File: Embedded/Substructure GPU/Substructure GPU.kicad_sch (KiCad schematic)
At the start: 30 parts, among them J1 10171746-00021LF, J11 Substructure Power, J2 HUB75, J3 5V, U2 74HC245D_653, U3 74HC245D_653, U5 Substructure, U6 LD1117S33TR_SOT223, U7 LD1117S50TR_SOT223

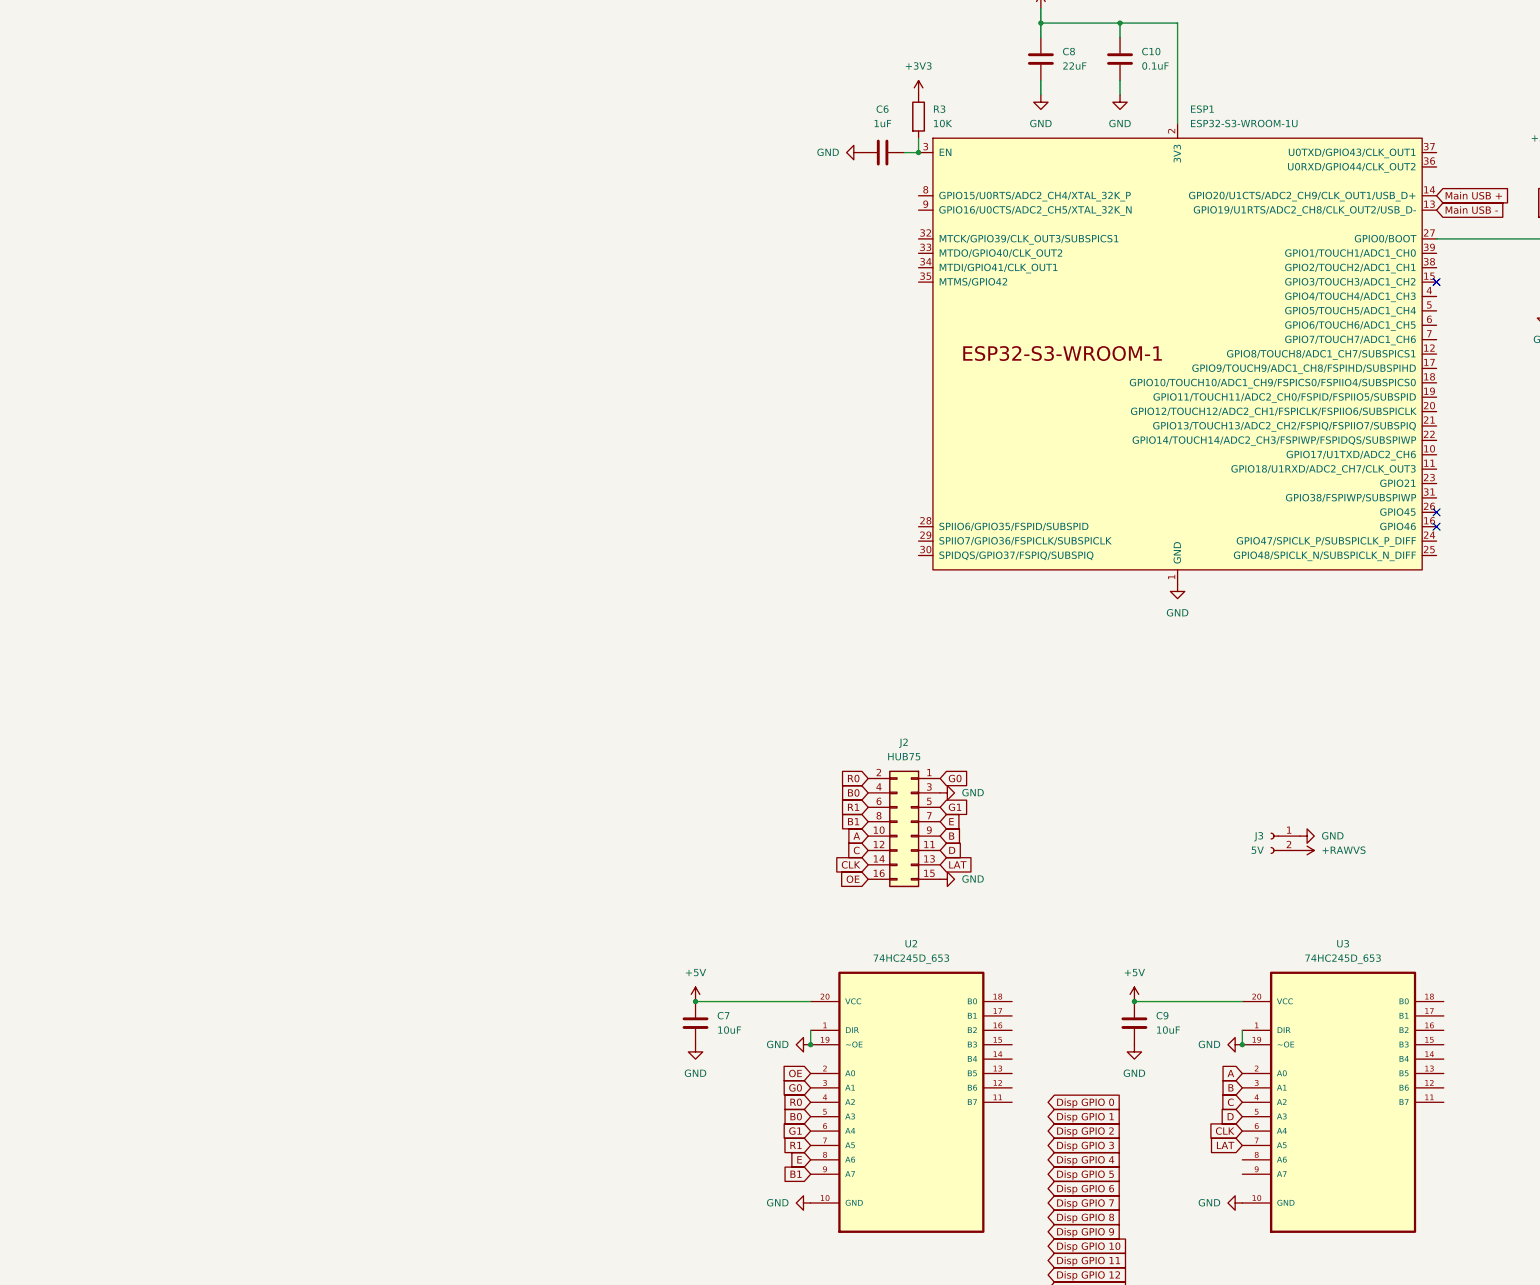
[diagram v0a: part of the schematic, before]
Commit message: Added Component placement for main systems
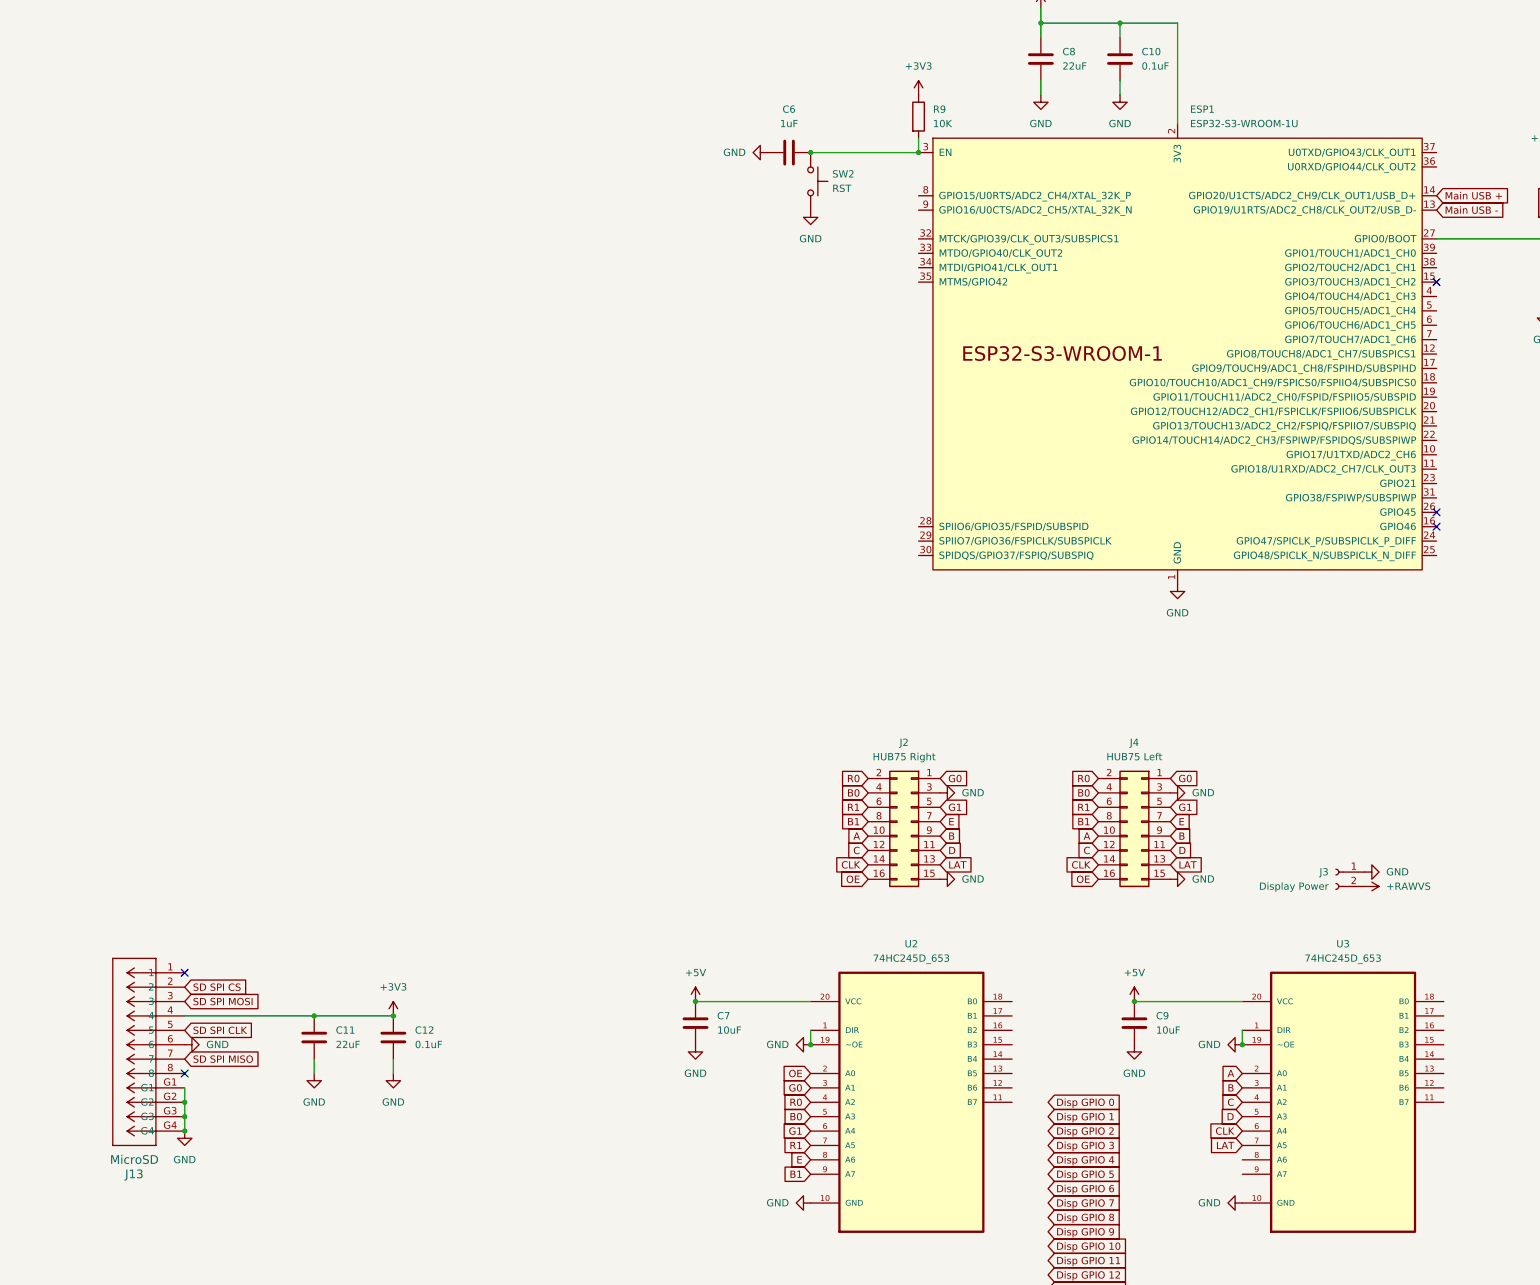
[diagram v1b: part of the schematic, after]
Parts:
- added C11: 22uF, Capacitor_SMD:C_0603_1608Metric_Pad1.08x0.95mm_HandSolder, symbol Device:C
- added C12: 0.1uF, Capacitor_SMD:C_0603_1608Metric_Pad1.08x0.95mm_HandSolder, symbol Device:C
- added J13: MicroSD, Micro SD:MicroSD_473092651, symbol MicroSD_473092651:473092651
- added J4: HUB75 Left, Connector_PinHeader_2.54mm:PinHeader_2x08_P2.54mm_Vertical, symbol Connector_Generic:Conn_02x08_Odd_Even
- added SW2: RST, Buttons:R-667843, symbol Switch:SW_Push
- J11: footprint Connector_AMASS:AMASS_XT30PW-M_1x02_P2.50mm_Horizontal -> Connector_AMASS:AMASS_XT30U-M_1x02_P5.0mm_Vertical
- J2: value HUB75 -> HUB75 Right
- J3: value 5V -> Display Power; footprint Connector_AMASS:AMASS_XT30PW-M_1x02_P2.50mm_Horizontal -> Connector_AMASS:AMASS_XT30U-M_1x02_P5.0mm_Vertical
- U2, U3: footprint 74HC245D:SOIC127P1032X265-20N -> 74HC245:SOIC127P1032X265-20N
- renumbered R3 to R9
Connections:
- net +3V3: now also C11.1, C12.1, J13.4
- net A: now also J4.10 (Pin_10)
- net B: now also J4.9 (Pin_9)
- net B0: now also J4.4 (Pin_4)
- net B1: now also J4.8 (Pin_8)
- net C: now also J4.12 (Pin_12)
- net CLK: now also J4.14 (Pin_14)
- net D: now also J4.11 (Pin_11)
- net E: now also J4.7 (Pin_7)
- net G0: now also J4.1 (Pin_1)
- net G1: now also J4.5 (Pin_5)
- net GND: now also C11.2, C12.2, J13.6, J13.G1, J13.G2, J13.G3, J13.G4, J4.15 (Pin_15), J4.3 (Pin_3), SW2.2
- net LAT: now also J4.13 (Pin_13)
- net OE: now also J4.16 (Pin_16)
- net R0: now also J4.2 (Pin_2)
- net R1: now also J4.6 (Pin_6)
- net at C6.2, ESP1.3 (EN), R9.2: now also SW2.1
- new net SD SPI CLK: J13.5
- new net SD SPI CS: J13.2
- new net SD SPI MISO: J13.7
- new net SD SPI MOSI: J13.3
- no-connect marks 9 -> 11
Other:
- moved on the sheet: C6, J3

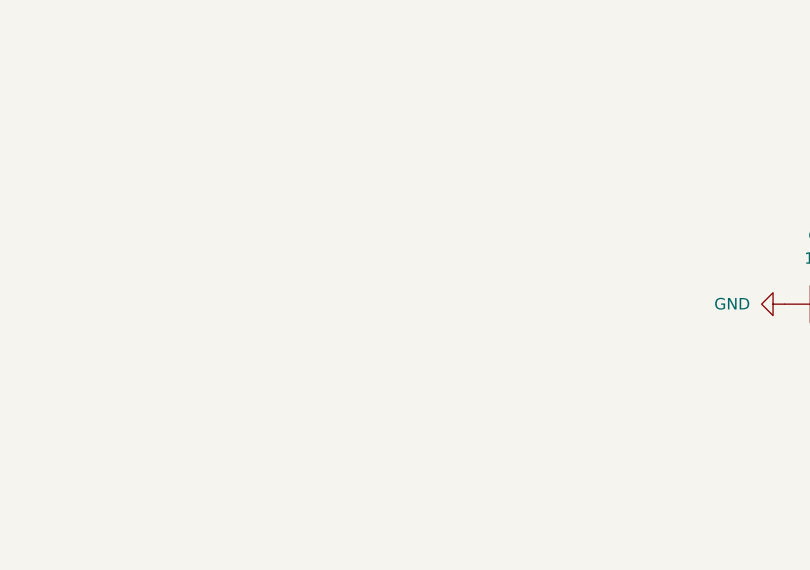
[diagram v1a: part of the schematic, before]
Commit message: Added Pins to route in schematic
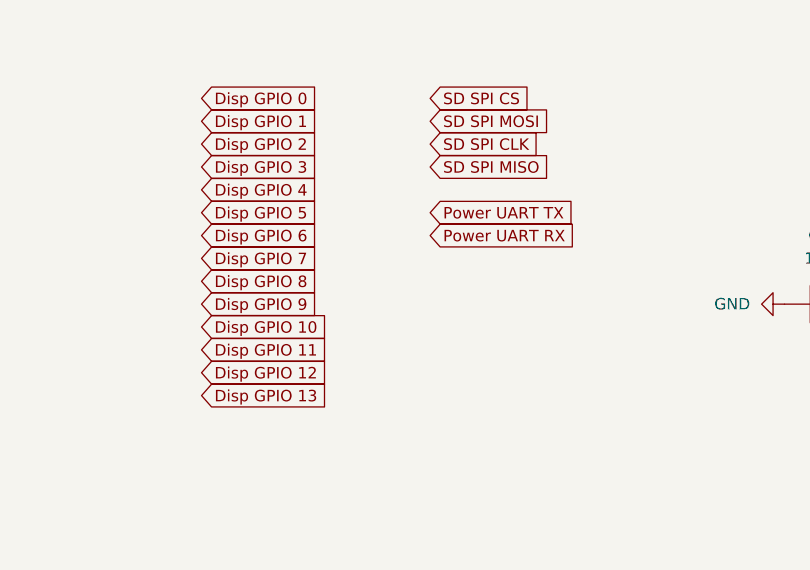
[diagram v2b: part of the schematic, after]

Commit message: Added GPU Routing
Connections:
- net +5VS is gone; now on net +RAWVS: C1.1, C2.1, U6.3 (VI), U7.3 (VI)
- net A: now also U2.8 (A6); no longer U3.2 (A0)
- net B: now also U2.7 (A5); no longer U3.3 (A1)
- net B0: now also U3.5 (A3); no longer U2.5 (A3)
- net B1: now also U3.8 (A6); no longer U2.9 (A7)
- net C: now also U2.6 (A4); no longer U3.4 (A2)
- net CLK: now also U2.4 (A2); no longer U3.6 (A4)
- net D: now also U2.5 (A3); no longer U3.5 (A3)
- net Disp GPIO 0: now also ESP1.28 (SPIIO6/GPIO35/FSPID/SUBSPID), U2.18 (B0)
- net Disp GPIO 1: now also ESP1.29 (SPIIO7/GPIO36/FSPICLK/SUBSPICLK), U2.17 (B1)
- net Disp GPIO 10: now also ESP1.8 (GPIO15/U0RTS/ADC2_CH4/XTAL_32K_P), U3.16 (B2)
- net Disp GPIO 11: now also ESP1.9 (GPIO16/U0CTS/ADC2_CH5/XTAL_32K_N), U3.15 (B3)
- net Disp GPIO 12: now also ESP1.10 (GPIO17/U1TXD/ADC2_CH6), U3.14 (B4)
- net Disp GPIO 13: now also ESP1.11 (GPIO18/U1RXD/ADC2_CH7/CLK_OUT3), U3.13 (B5)
- net Disp GPIO 2: now also ESP1.30 (SPIDQS/GPIO37/FSPIQ/SUBSPIQ), U2.16 (B2)
- net Disp GPIO 3: now also ESP1.31 (GPIO38/FSPIWP/SUBSPIWP), U2.15 (B3)
- net Disp GPIO 4: now also ESP1.32 (MTCK/GPIO39/CLK_OUT3/SUBSPICS1), U2.14 (B4)
- net Disp GPIO 5: now also ESP1.33 (MTDO/GPIO40/CLK_OUT2), U2.13 (B5)
- net Disp GPIO 6: now also ESP1.34 (MTDI/GPIO41/CLK_OUT1), U2.12 (B6)
- net Disp GPIO 7: now also ESP1.35 (MTMS/GPIO42), U2.11 (B7)
- net Disp GPIO 8: now also ESP1.6 (GPIO6/TOUCH6/ADC1_CH5), U3.18 (B0)
- net Disp GPIO 9: now also ESP1.7 (GPIO7/TOUCH7/ADC1_CH6), U3.17 (B1)
- net E: now also U2.9 (A7); no longer U2.8 (A6)
- net G0: now also U3.4 (A2); no longer U2.3 (A1)
- net G1: now also U3.7 (A5); no longer U2.6 (A4)
- net LAT: now also U2.3 (A1); no longer U3.7 (A5)
- net R0: now also U3.3 (A1); no longer U2.4 (A2)
- net R1: now also U3.6 (A4); no longer U2.7 (A5)
- net SD SPI CLK: now also ESP1.18 (GPIO10/TOUCH10/ADC1_CH9/FSPICS0/FSPIIO4/SUBSPICS0)
- net SD SPI CS: now also ESP1.20 (GPIO12/TOUCH12/ADC2_CH1/FSPICLK/FSPIIO6/SUBSPICLK)
- net SD SPI MISO: now also ESP1.17 (GPIO9/TOUCH9/ADC1_CH8/FSPIHD/SUBSPIHD)
- net SD SPI MOSI: now also ESP1.19 (GPIO11/TOUCH11/ADC2_CH0/FSPID/FSPIIO5/SUBSPID)
- net Disp GPIO 14: now reaches ESP1.12 (GPIO8/TOUCH8/ADC1_CH7/SUBSPICS1)
- net Disp GPIO 14: now also U3.12 (B6)
- net OE renamed OE0
- net OE0: no longer J2.16 (Pin_16)
- new net OE1: J2.16 (Pin_16), U3.2 (A0)
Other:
- moved on the sheet: C6, SW2

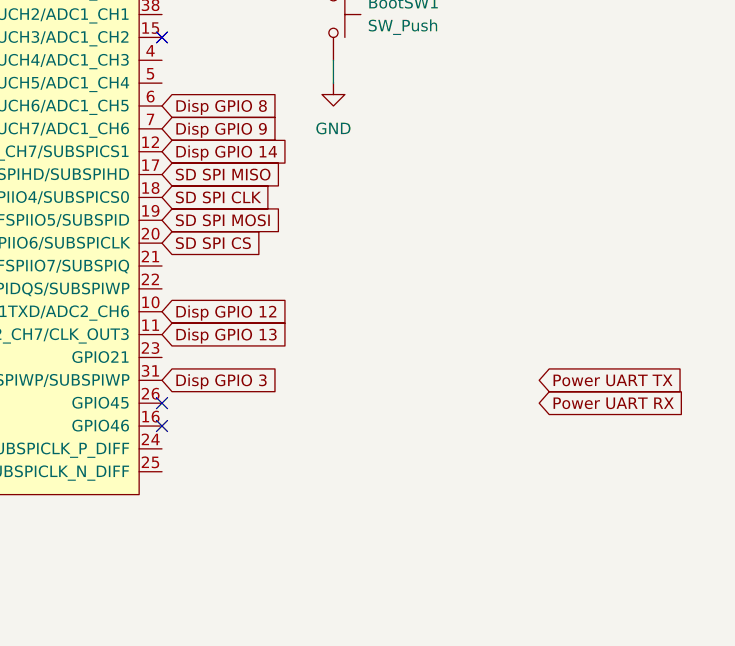
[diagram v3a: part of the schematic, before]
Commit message: Added New Routing (Improved board space & signal noise)
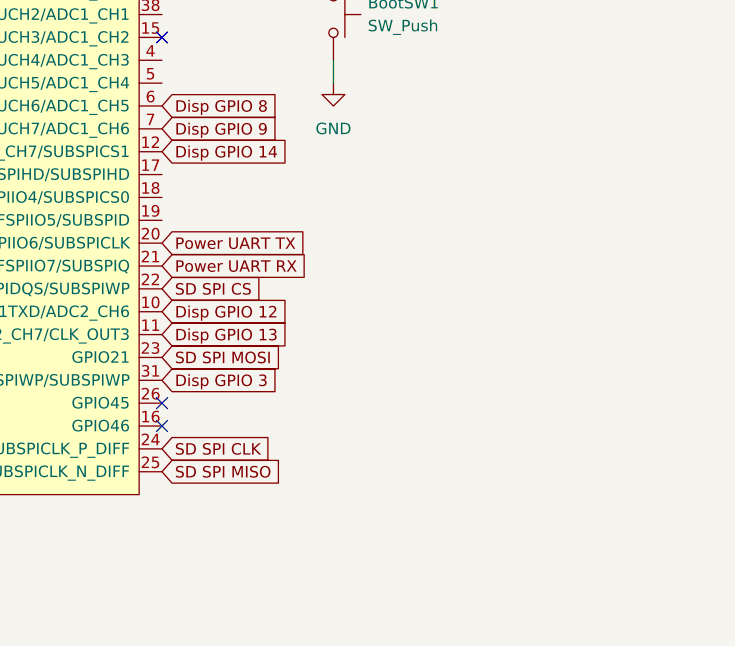
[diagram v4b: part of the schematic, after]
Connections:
- net Power UART RX: now also ESP1.21 (GPIO13/TOUCH13/ADC2_CH2/FSPIQ/FSPIIO7/SUBSPIQ)
- net Power UART TX: now also ESP1.20 (GPIO12/TOUCH12/ADC2_CH1/FSPICLK/FSPIIO6/SUBSPICLK)
- net SD SPI CLK: now also ESP1.24 (GPIO47/SPICLK_P/SUBSPICLK_P_DIFF); no longer ESP1.18 (GPIO10/TOUCH10/ADC1_CH9/FSPICS0/FSPIIO4/SUBSPICS0)
- net SD SPI CS: now also ESP1.22 (GPIO14/TOUCH14/ADC2_CH3/FSPIWP/FSPIDQS/SUBSPIWP); no longer ESP1.20 (GPIO12/TOUCH12/ADC2_CH1/FSPICLK/FSPIIO6/SUBSPICLK)
- net SD SPI MISO: now also ESP1.25 (GPIO48/SPICLK_N/SUBSPICLK_N_DIFF); no longer ESP1.17 (GPIO9/TOUCH9/ADC1_CH8/FSPIHD/SUBSPIHD)
- net SD SPI MOSI: now also ESP1.23 (GPIO21); no longer ESP1.19 (GPIO11/TOUCH11/ADC2_CH0/FSPID/FSPIIO5/SUBSPID)

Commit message: Modified Display pins (Corrected port orientation) & Added Silkscreen Data
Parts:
- added J5: Expansion Data, Connector_PinSocket_2.54mm:PinSocket_1x04_P2.54mm_Vertical, symbol Connector_Generic:Conn_01x04
- added J6: Expansion PWR, Connector_PinSocket_2.54mm:PinSocket_1x04_P2.54mm_Vertical, symbol Connector_Generic:Conn_01x04
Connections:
- net +RAWVS: now also J6.2 (Pin_2), J6.3 (Pin_3)
- net A: now also J2.9 (Pin_9), J4.9 (Pin_9); no longer J2.10 (Pin_10), J4.10 (Pin_10)
- net B: now also J2.10 (Pin_10), J4.10 (Pin_10); no longer J2.9 (Pin_9), J4.9 (Pin_9)
- net B0: now also J2.3 (Pin_3), J4.3 (Pin_3); no longer J2.4 (Pin_4), J4.4 (Pin_4)
- net B1: now also J2.7 (Pin_7), J4.7 (Pin_7); no longer J2.8 (Pin_8), J4.8 (Pin_8)
- net C: now also J2.11 (Pin_11), J4.11 (Pin_11); no longer J2.12 (Pin_12), J4.12 (Pin_12)
- net CLK: now also J2.13 (Pin_13), J4.13 (Pin_13); no longer J2.14 (Pin_14), J4.14 (Pin_14)
- net D: now also J2.12 (Pin_12), J4.12 (Pin_12); no longer J2.11 (Pin_11), J4.11 (Pin_11)
- net E: now also J2.8 (Pin_8), J4.8 (Pin_8); no longer J2.7 (Pin_7), J4.7 (Pin_7)
- net G0: now also J2.2 (Pin_2), J4.2 (Pin_2); no longer J2.1 (Pin_1), J4.1 (Pin_1)
- net G1: now also J2.6 (Pin_6), J4.6 (Pin_6); no longer J2.5 (Pin_5), J4.5 (Pin_5)
- net GND: now also J2.16 (Pin_16), J2.4 (Pin_4), J4.16 (Pin_16), J4.4 (Pin_4), J5.1 (Pin_1), J5.4 (Pin_4), J6.1 (Pin_1), J6.4 (Pin_4); no longer J2.15 (Pin_15), J2.3 (Pin_3), J4.15 (Pin_15), J4.3 (Pin_3)
- net LAT: now also J2.14 (Pin_14), J4.14 (Pin_14); no longer J2.13 (Pin_13), J4.13 (Pin_13)
- net OE0: now also J4.15 (Pin_15); no longer J4.16 (Pin_16)
- net OE1: now also J2.15 (Pin_15); no longer J2.16 (Pin_16)
- net R0: now also J2.1 (Pin_1), J4.1 (Pin_1); no longer J2.2 (Pin_2), J4.2 (Pin_2)
- net R1: now also J2.5 (Pin_5), J4.5 (Pin_5); no longer J2.6 (Pin_6), J4.6 (Pin_6)
- net Expansion UART TX: now reaches ESP1.38 (GPIO2/TOUCH2/ADC1_CH1)
- net Expansion UART TX: now also J5.3 (Pin_3)
- net Expansion UART RX: now reaches ESP1.39 (GPIO1/TOUCH1/ADC1_CH0)
- net Expansion UART RX: now also J5.2 (Pin_2)
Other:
- moved on the sheet: BootSW1, C10, C6, C8, ESP1, R4, R9, SW2
